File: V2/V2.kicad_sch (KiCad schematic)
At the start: 9 parts, among them U1 MLX91221KDC-ABR-050-RE, U2 ADS1115IDGSR, U3 HLK-PM01, U4 ESP32-S3-MINI-1-N8

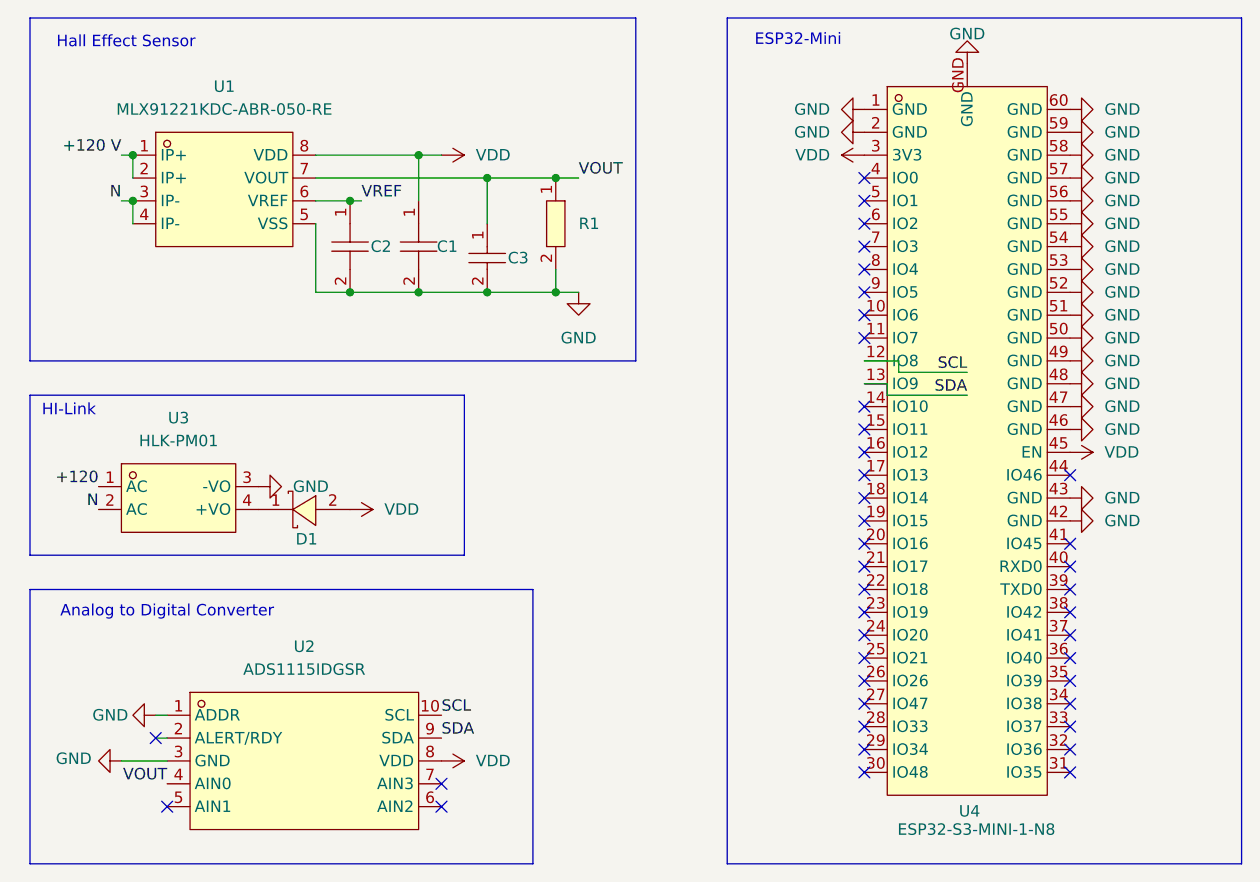
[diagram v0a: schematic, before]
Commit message: fixed diode
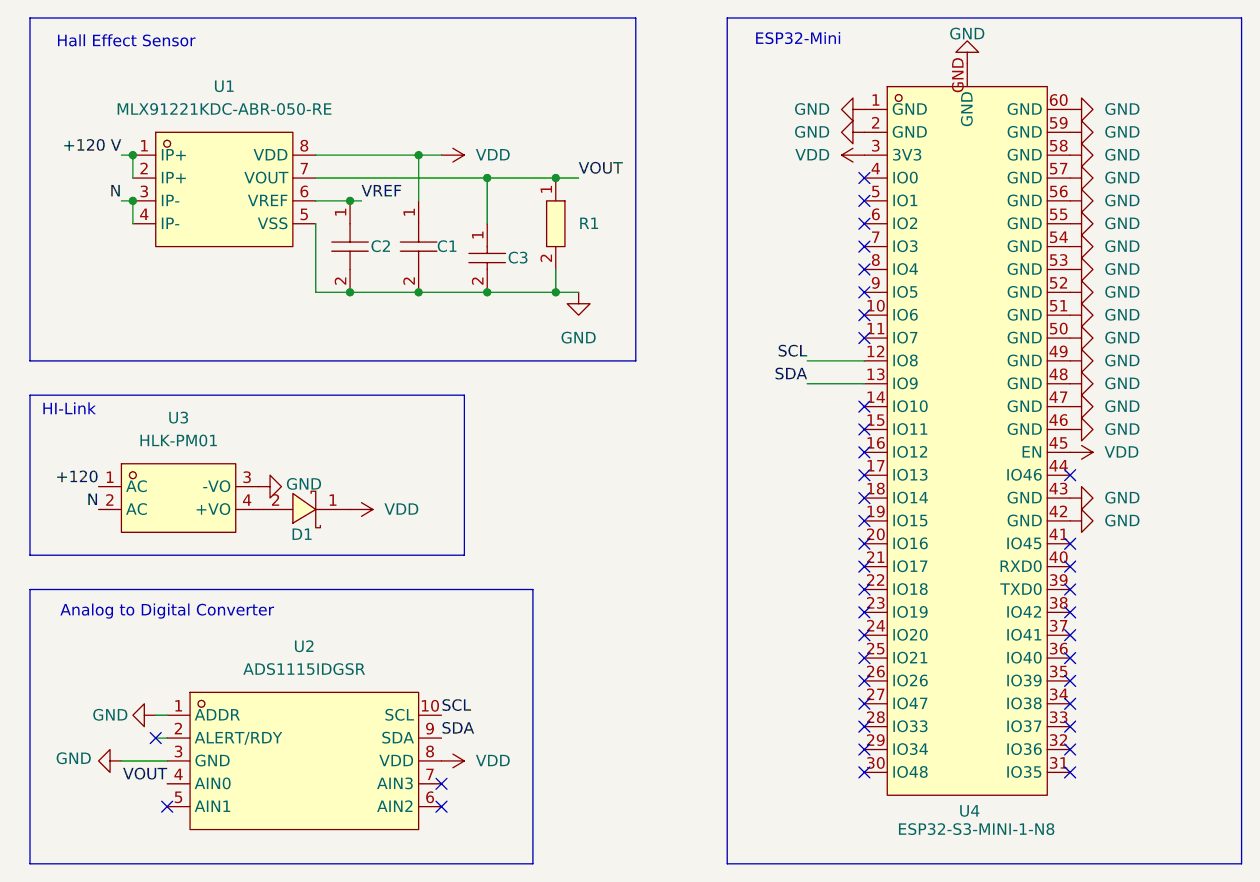
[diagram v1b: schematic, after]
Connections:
- net VDD: now also D1.1 (C); no longer D1.2 (A)
- net at U3.4 (+VO): now also D1.2 (A); no longer D1.1 (C)
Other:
- moved on the sheet: D1
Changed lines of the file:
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@@
 	(wire
 		(pts
-			(xy 110.49 62.23) (xy 114.3 62.23)
+			(xy 110.49 64.77) (xy 104.14 64.77)
 		)
 		(stroke
@@
 	(wire
 		(pts
-			(xy 114.3 63.5) (xy 121.92 63.5)
+			(xy 68.58 54.61) (xy 76.2 54.61)
 		)
 		(stroke
@@
 	(wire
 		(pts
-			(xy 113.03 66.04) (xy 121.92 66.04)
+			(xy 76.2 41.91) (xy 78.74 41.91)
 		)
 		(stroke
@@
 	(wire
 		(pts
-			(xy 68.58 54.61) (xy 76.2 54.61)
+			(xy 49.53 46.99) (xy 49.53 54.61)
 		)
 		(stroke
@@
 	(wire
 		(pts
-			(xy 76.2 41.91) (xy 78.74 41.91)
+			(xy 110.49 62.23) (xy 104.14 62.23)
 		)
 		(stroke
@@
 	(wire
 		(pts
-			(xy 49.53 46.99) (xy 49.53 54.61)
+			(xy 29.21 44.45) (xy 29.21 46.99)
 		)
 		(stroke
@@
 	(wire
 		(pts
-			(xy 29.21 44.45) (xy 29.21 46.99)
+			(xy 60.96 39.37) (xy 60.96 44.45)
 		)
 		(stroke
@@
 	(wire
 		(pts
-			(xy 60.96 39.37) (xy 60.96 44.45)
+			(xy 49.53 54.61) (xy 53.34 54.61)
 		)
 		(stroke
@@
 	(wire
 		(pts
-			(xy 49.53 54.61) (xy 53.34 54.61)
+			(xy 53.34 54.61) (xy 60.96 54.61)
 		)
 		(stroke
@@
 	(wire
 		(pts
-			(xy 53.34 54.61) (xy 60.96 54.61)
+			(xy 27.94 44.45) (xy 29.21 44.45)
 		)
 		(stroke
@@
 	(wire
 		(pts
-			(xy 114.3 62.23) (xy 114.3 63.5)
+			(xy 53.34 44.45) (xy 54.61 44.45)
 		)
 		(stroke
@@
 	(wire
 		(pts
-			(xy 27.94 44.45) (xy 29.21 44.45)
+			(xy 60.96 54.61) (xy 68.58 54.61)
 		)
 		(stroke
@@
 	(wire
 		(pts
-			(xy 53.34 44.45) (xy 54.61 44.45)
+			(xy 60.96 39.37) (xy 63.5 39.37)
 		)
 		(stroke
@@
 	(wire
 		(pts
-			(xy 60.96 54.61) (xy 68.58 54.61)
-		)
-		(stroke
-			(width 0)
-			(type default)
-		)
-	)
-	(wire
-		(pts
-			(xy 60.96 39.37) (xy 63.5 39.37)
-		)
-		(stroke
-			(width 0)
-			(type default)
-		)
-	)
-	(wire
-		(pts
 			(xy 68.58 41.91) (xy 76.2 41.91)
-		)
-		(stroke
-			(width 0)
-			(type default)
-		)
-	)
-	(wire
-		(pts
-			(xy 113.03 64.77) (xy 113.03 66.04)
-		)
-		(stroke
-			(width 0)
-			(type default)
-		)
-	)
-	(wire
-		(pts
-			(xy 110.49 64.77) (xy 113.03 64.77)
 		)
 		(stroke
@@
 	)
 	(label "SCL"
-		(at 121.92 63.5 180)
+		(at 104.14 62.23 180)
 		(effects
 			(font
@@
 	)
 	(label "SDA"
-		(at 121.92 66.04 180)
+		(at 104.14 64.77 180)
 		(effects
 			(font
@@
 		(on_board yes)
 		(dnp no)
-		(fields_autoplaced yes)
 		(property "Reference" "#PWR06"
 			(at 49.53 76.2 0)
@@
 		)
 		(property "Value" "GND"
-			(at 46.99 76.1999 90)
+			(at 46.228 75.946 90)
 			(effects
 				(font
@@
 	(symbol
 		(lib_id "SS14:SS14_C466498")
-		(at 48.26 78.74 0)
+		(at 48.26 78.74 180)
 		(unit 1)
 		(exclude_from_sim no)
@@
 		(dnp no)
 		(property "Reference" "D1"
-			(at 48.514 82.042 0)
+			(at 48.006 81.534 0)
 			(effects
 				(font
@@
 		)
 		(property "Value" "SS14_C466498"
-			(at 48.005 74.93 0)
+			(at 48.515 82.55 0)
 			(effects
 				(font
@@
 		)
 		(property "Footprint" "SS14:SMA_L4.2-W2.6-LS5.3-RD"
-			(at 48.26 86.36 0)
+			(at 48.26 71.12 0)
 			(effects
 				(font
@@
 		)
 		(property "Datasheet" "https://lcsc.com/product-detail/Schottky-Barrier-Diodes-SBD_High-Diode-SS14_C466498.html"
-			(at 48.26 88.9 0)
+			(at 48.26 68.58 0)
 			(effects
 				(font
@@
 		)
 		(property "LCSC Part" "C466498"
-			(at 48.26 91.44 0)
-			(effects
-				(font
+			(at 48.26 66.04 0)
+			(effects
+				(font

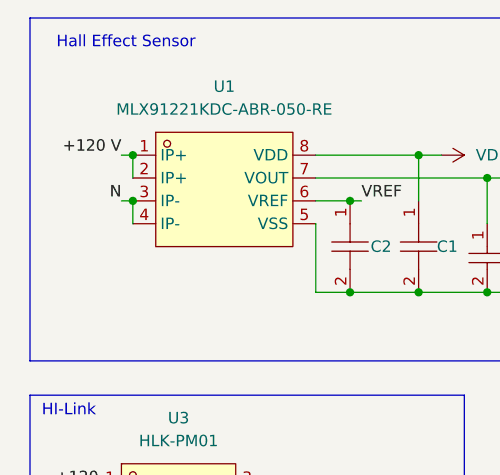
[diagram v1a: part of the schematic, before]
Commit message: added capacitor values and fixed the input of  ip-
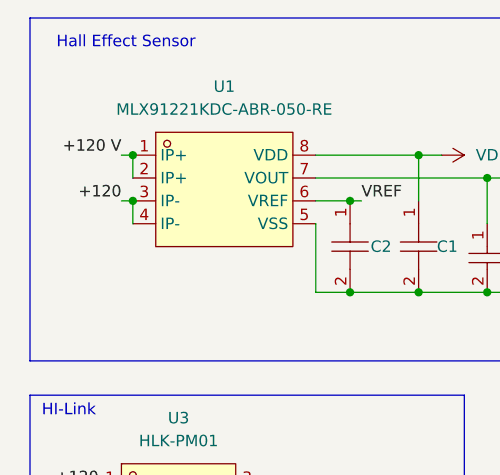
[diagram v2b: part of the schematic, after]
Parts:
- C1, C2: value CL05B473KB5VPNC -> 47nF
- C3: value GRM1885C1H472JA01D -> 4.7nF
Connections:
- net +120: now also U1.3 (IP-), U1.4 (IP-)
- net N: no longer U1.3 (IP-), U1.4 (IP-)
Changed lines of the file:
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@@
 		)
 	)
-	(label "N"
+	(label "+120"
 		(at 27.94 44.45 180)
 		(effects
@@
 			)
 		)
-		(property "Value" "GRM1885C1H472JA01D"
+		(property "Value" "4.7nF"
 			(at 72.39 50.8 0)
 			(effects
@@
 			)
 		)
-		(property "Value" "CL05B473KB5VPNC"
+		(property "Value" "47nF"
 			(at 64.77 50.7999 0)
 			(effects
@@
 			)
 		)
-		(property "Value" "CL05B473KB5VPNC"
+		(property "Value" "47nF"
 			(at 57.15 50.7999 0)
 			(effects
